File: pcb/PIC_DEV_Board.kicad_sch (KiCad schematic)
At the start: 8 parts, among them J1 Conn_01x08_Pin, J3 Conn_01x15_Pin, J4 Conn_01x02_Pin

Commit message: higher functionality board
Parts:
- removed J3: Conn_01x15_Pin, Connector_PinHeader_2.54mm:PinHeader_1x15_P2.54mm_Vertical, symbol Connector:Conn_01x15_Pin
- added C2, C3: 30pF, Capacitor_SMD:C_0805_2012Metric, symbol Device:C
- added C4, C6, C8: 0.1uF, Capacitor_SMD:C_0805_2012Metric, symbol Device:C
- added C5, C7, C9: 10uF, Capacitor_SMD:C_0805_2012Metric, symbol Device:C
- added D2, D3, D4, D5, D6, D7, D8, D9: LED, LED_SMD:LED_0805_2012Metric, symbol Device:LED
- added J2: USB_A, Connector_USB:USB_A_Receptacle_GCT_USB1046, symbol Connector:USB_A
- added R10, R4, R5, R6, R7, R8, R9: 10K, Resistor_SMD:R_0805_2012Metric, symbol Device:R
- added R11, R12, R13, R14, R15, R16, R17, R18: 560, Resistor_SMD:R_0805_2012Metric, symbol Device:R
- added R3: 0, Resistor_SMD:R_0805_2012Metric, symbol Device:R
- added U2: ~, Package_SO:SOIC-8_3.9x4.9mm_P1.27mm, symbol myCustomParts:AT24C01D
- added U3: MCP3002, Package_SO:SOIC-8_3.9x4.9mm_P1.27mm, symbol Analog_ADC:MCP3002
- added U4: MCP4801, Package_SO:SOIC-8_3.9x4.9mm_P1.27mm, symbol Analog_DAC:MCP4801
- added U5: FT230XS, Package_SO:SSOP-16_3.9x4.9mm_P0.635mm, symbol Interface_USB:FT230XS
- added U6: 74HC595, Package_SO:SOIC-16_3.9x9.9mm_P1.27mm, symbol 74xx:74HC595
- added Y1: Crystal, symbol Device:Crystal
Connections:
- net Earth: now also C2.1, C3.1, C4.2, C5.1, C6.2, C7.1, C8.2, C9.1, D2.1 (K), D3.1 (K), D4.1 (K), D5.1 (K), D6.1 (K), D7.1 (K), D8.1 (K), D9.1 (K), R10.1, R3.1, R8.1, R9.1, U2.4 (GND), U3.4 (VSS), U4.7 (Vss), U5.13 (GND), U5.5 (GND), U6.8 (GND)
- net +3V3: now reaches C1.2, J1.2 (Pin_2), J4.2 (Pin_2), R1.1, R2.1, U1.1 (Vdd)
- net +3V3: now also C4.1, C5.2, C6.1, C7.2, C8.1, C9.2, R4.1, R5.1, R6.1, R7.1, U2.8 (Vcc), U3.8 (VDD/VREF), U4.1 (Vdd), U5.12 (VCC), U6.16 (VCC)
- net Vpp/RA3/MCLR: now reaches R1.2, U1.4 (Vpp/RA3/MCLR)
- net Vpp/RA3/MCLR: no longer J1.1 (Pin_1)
- net at U1.2 (RA5): now also C2.2, Y1.2
- net at U1.16 (RC0): now also U5.4 (RXD)
- net at U1.15 (RC1): now also U6.14 (SER)
- net at U1.14 (RC2): now also U6.11 (SRCLK)
- net at U1.13 (RB4): now also U2.5 (SDA)
- net at U1.11 (RB6): now also U2.6 (SCL)
- net at U1.3 (RA4): now also C3.2, Y1.1
- net ~{DAC_CS}: now reaches U1.6 (RC4)
- net ~{DAC_CS}: now also U4.2 (~{CS})
- net ~{ADC_CS}: now reaches U1.7 (RC3)
- net ~{ADC_CS}: now also U3.1 (~{CS}/SHDN)
- net SCK: now reaches U1.8 (RC6)
- net SCK: now also U3.7 (CLK), U4.3 (SCK)
- net SDO: now reaches U1.9 (RC7)
- net SDO: now also U3.6 (DOUT)
- net SDI: now reaches U1.10 (RB7)
- net SDI: now also U3.5 (DIN), U4.4 (SDI)
- net at U1.17 (RA2): now also U5.1 (TXD)
- new net: D5.2 (A), R14.2
- new net: R6.2, R9.2, U2.2 (A1)
- new net: J2.3 (D+), U5.8 (USBDP)
- new net: J2.2 (D-), U5.9 (USBDM)
- new net: R14.1, U6.3 (QD)
- new net: R15.1, U6.4 (QE)
- new net: D6.2 (A), R15.2
- new net: R3.2, R4.2, U2.7 (WP)
- new net: D2.2 (A), R11.2
- new net: D4.2 (A), R13.2
- new net: R10.2, R7.2, U2.3 (A2)
- new net: D7.2 (A), R16.2
- new net: R16.1, U6.5 (QF)
- new net: D8.2 (A), R17.2
- new net: R5.2, R8.2, U2.1 (A0)
- new net: R13.1, U6.2 (QC)
- new net: R17.1, U6.6 (QG)
- new net: R11.1, U6.15 (QA)
- new net: R12.1, U6.1 (QB)
- new net: R18.1, U6.7 (QH)
- new net: D9.2 (A), R18.2
- new net: D3.2 (A), R12.2
- new net Vpp/RA3/MCLR: J1.1 (Pin_1)
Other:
- moved on the sheet: D1, J1, R1, R2

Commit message: size reduction
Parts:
- removed C2, C3: 30pF, Capacitor_SMD:C_0805_2012Metric, symbol Device:C
- removed D3, D4, D5, D6, D7, D8, D9: LED, LED_SMD:LED_0805_2012Metric, symbol Device:LED
- removed J2: USB_A, Connector_USB:USB_A_Receptacle_GCT_USB1046, symbol Connector:USB_A
- removed R10, R4, R5, R6, R7, R8, R9: 10K, Resistor_SMD:R_0805_2012Metric, symbol Device:R
- removed R11, R12, R13, R14, R15, R16, R17, R18: 560, Resistor_SMD:R_0805_2012Metric, symbol Device:R
- removed U6: 74HC595, Package_SO:SOIC-16_3.9x9.9mm_P1.27mm, symbol 74xx:74HC595
- removed Y1: Crystal, symbol Device:Crystal
- added J3: Conn_01x02_Pin, Connector_PinHeader_2.54mm:PinHeader_1x02_P2.54mm_Vertical, symbol Connector:Conn_01x02_Pin
- added J5: Conn_01x01_Pin, Connector_PinHeader_2.54mm:PinHeader_1x01_P2.54mm_Vertical, symbol Connector:Conn_01x01_Pin
- added U6: ~, myCustomFootprints:USB-A1HSB6, symbol myCustomParts:USB-A1HSB6
- R3: value 0 -> 1K
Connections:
- net Earth: now also U2.1 (A0), U2.2 (A1), U2.3 (A2), U2.7 (WP), U6.4 (GND); no longer R3.1
- net at U5.8 (USBDP): now also U6.3 (DP)
- net at U5.9 (USBDM): now also U6.2 (DM)
- net at R3.2: now also D2.2 (A); no longer U2.7 (WP)
- net at U4.8 (Vout): now also J5.1 (Pin_1)
- net at U1.2 (RA5): now also R3.1
- net at U3.2 (CH0): now also J3.1 (Pin_1)
- net at U3.3 (CH1): now also J3.2 (Pin_2)
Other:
- moved on the sheet: C4, C5, C6, C7, R1, U3, U4

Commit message: layout changes
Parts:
- added C2: 0.1uF, Capacitor_SMD:C_0805_2012Metric, symbol Device:C
- added R4: 10K, Resistor_SMD:R_0805_2012Metric, symbol Device:R
- added R5: 4.7K, Resistor_SMD:R_0805_2012Metric, symbol Device:R
- added TP1, TP2: TestPoint, TestPoint:TestPoint_Pad_1.5x1.5mm, symbol Connector:TestPoint
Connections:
- net Earth: now also C2.2, R4.1
- net at U1.17 (RA2), U5.1 (TXD): now also TP2.1
- net at U5.10 (3V3OUT): now also U5.11 (~{RESET}), U5.3 (VCCIO), C2.1
- net at U5.16 (CBUS3): now also R4.2, R5.1
- net at U1.16 (RC0), U5.4 (RXD): now also TP1.1
- net at U6.1 (VCC): now also R5.2

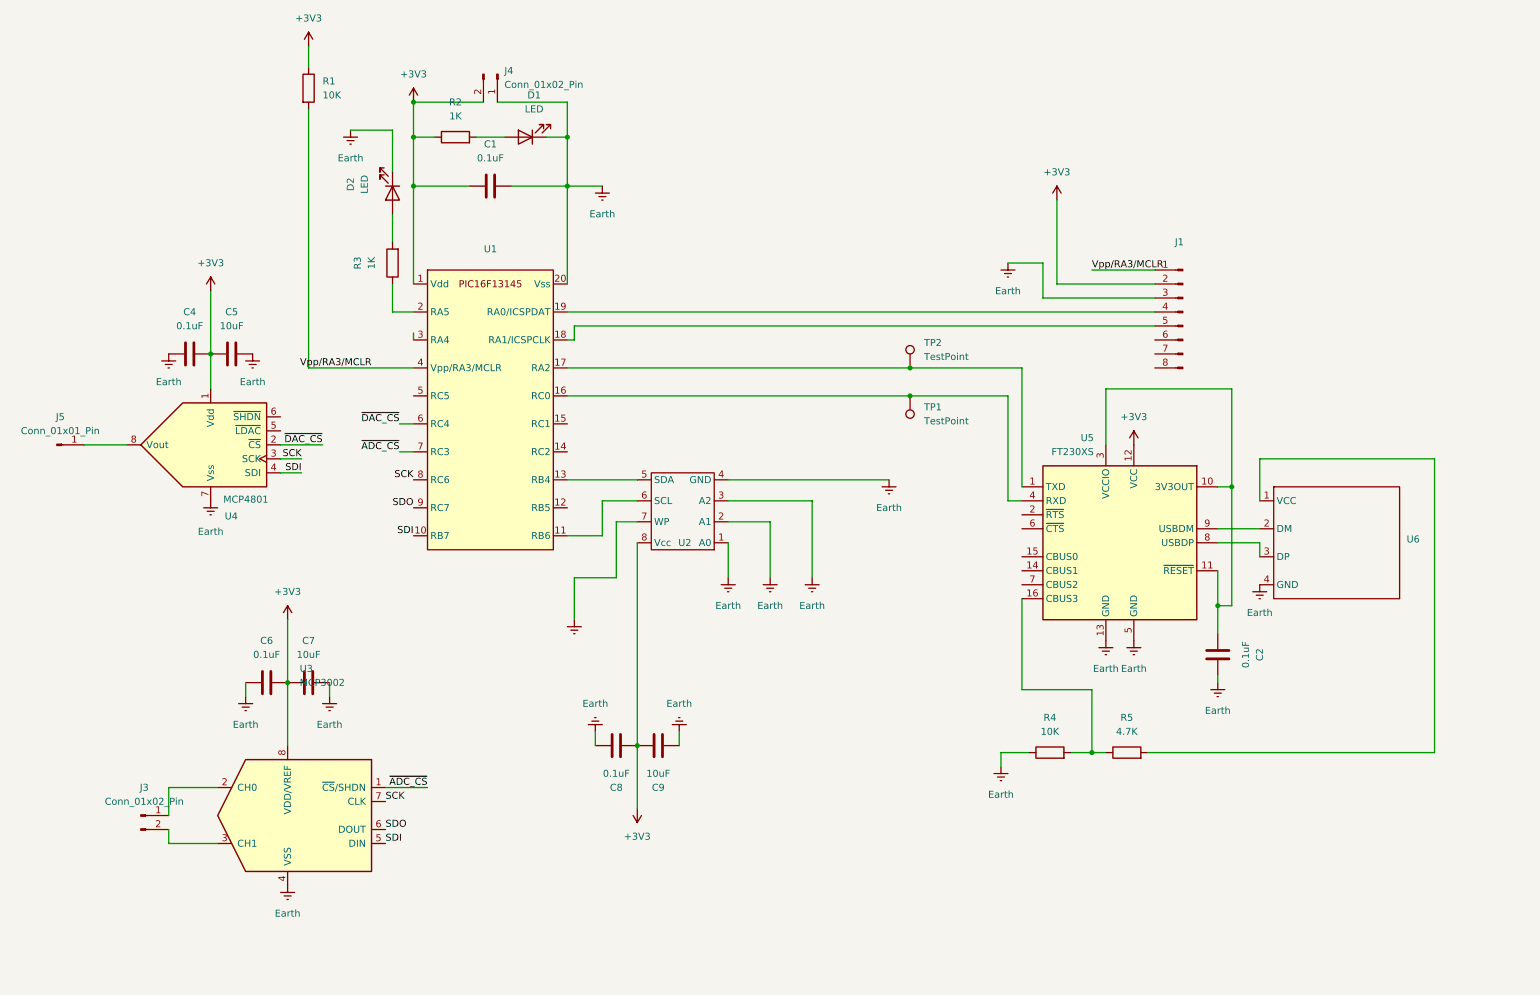
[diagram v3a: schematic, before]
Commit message: layout/schematic changes
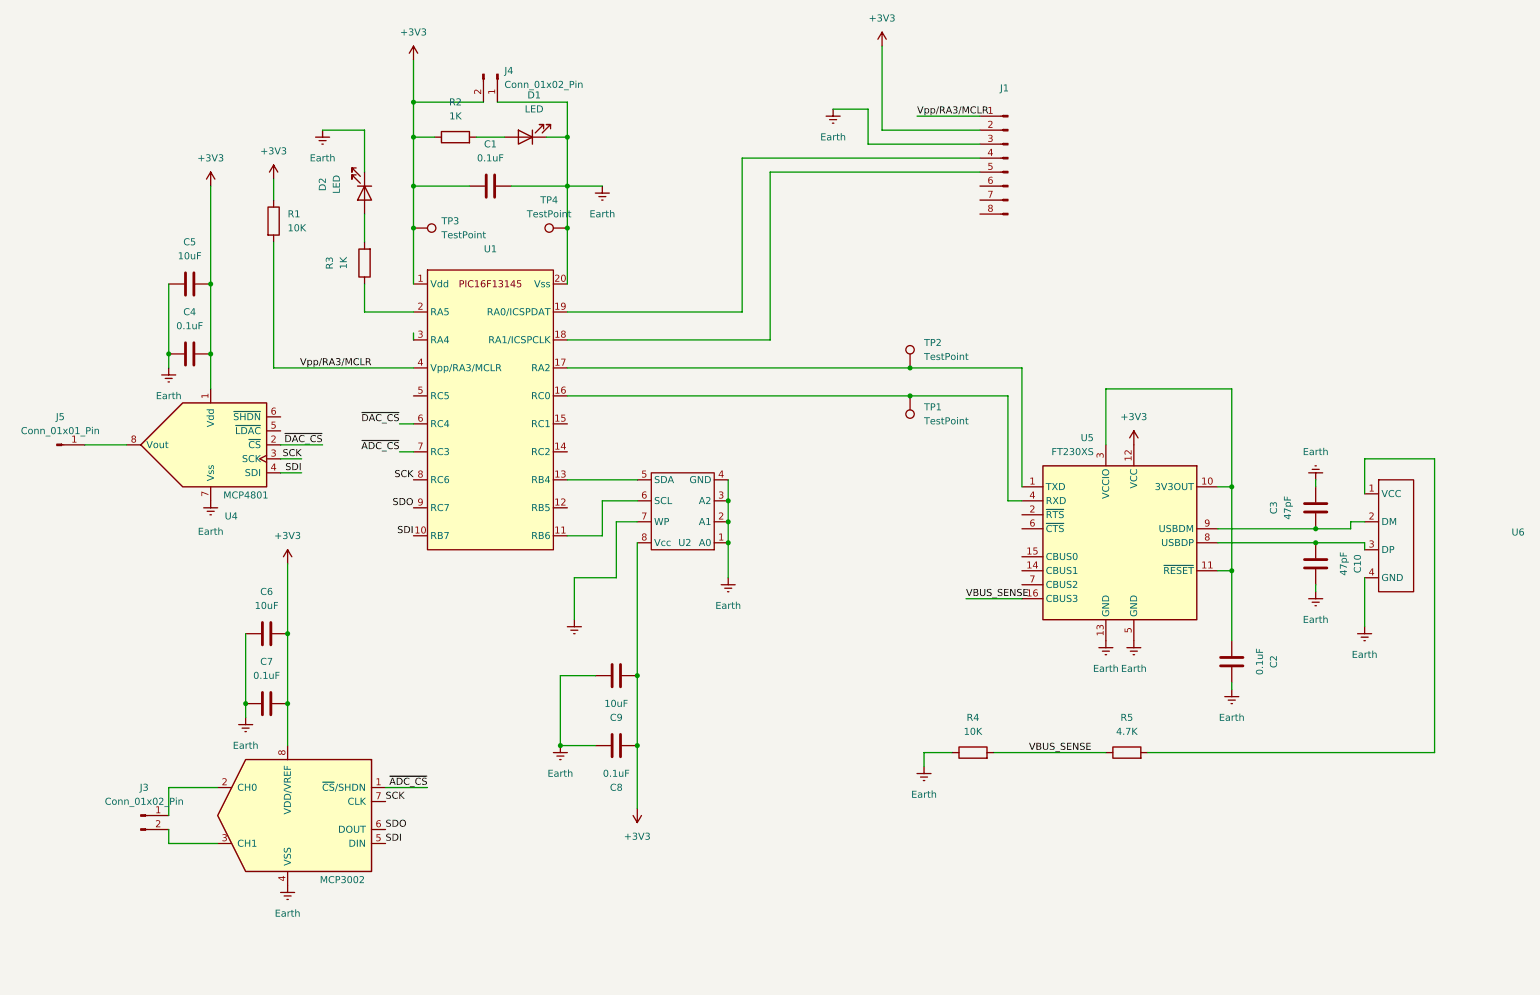
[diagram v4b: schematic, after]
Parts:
- added C10, C3: 47pF, Capacitor_SMD:C_0805_2012Metric, symbol Device:C
- added TP3, TP4: TestPoint, TestPoint:TestPoint_Pad_1.5x1.5mm, symbol Connector:TestPoint
- C6: value 0.1uF -> 10uF
- C7: value 10uF -> 0.1uF
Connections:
- net +3V3: now also C5.1, C7.1, C9.1, TP3.1; no longer C5.2, C7.2, C9.2
- net Earth: now also C5.2, C7.2, C9.2, C10.2, C3.2, TP4.1; no longer C5.1, C7.1, C9.1
- net VBUS_SENSE: now reaches R4.2, R5.1, U5.16 (CBUS3)
- net at U5.8 (USBDP), U6.3 (DP): now also C10.1
- net at U5.9 (USBDM), U6.2 (DM): now also C3.1
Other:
- moved on the sheet: C2, D2, J1, R1, R3, R4, U6

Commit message: layout/via changes
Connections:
- net Earth: now also U6.1 (GND); no longer U6.4 (GND)
- net at C10.1, U5.8 (USBDP): now also U6.2 (DP); no longer U6.3 (DP)
- net at C3.1, U5.9 (USBDM): now also U6.3 (DM); no longer U6.2 (DM)
- net at R5.2: now also U6.4 (VCC); no longer U6.1 (VCC)

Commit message: layout/via changes
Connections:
- net at U4.5 (~{LDAC}): now also U1.5 (RC5)
- net at U4.6 (~{SHDN}): now also U1.3 (RA4)
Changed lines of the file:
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@@
+	(wire
+		(pts
+			(xy 76.2 97.79) (xy 76.2 91.44)
+		)
+		(stroke
+			(width 0)
+			(type default)
+		)
+	)
 	(wire
 		(pts
@@
 	(wire
 		(pts
+			(xy 76.2 91.44) (xy 87.63 91.44)
+		)
+		(stroke
+			(width 0)
+			(type default)
+		)
+	)
+	(wire
+		(pts
 			(xy 115.57 116.84) (xy 121.92 116.84)
 		)
@@
 	(wire
 		(pts
+			(xy 87.63 81.28) (xy 83.82 81.28)
+		)
+		(stroke
+			(width 0)
+			(type default)
+		)
+	)
+	(wire
+		(pts
 			(xy 152.4 50.8) (xy 152.4 81.28)
 		)
@@
 	(wire
 		(pts
-			(xy 87.63 80.01) (xy 87.63 81.28)
-		)
-		(stroke
-			(width 0)
-			(type default)
-		)
-	)
-	(wire
-		(pts
 			(xy 118.11 142.24) (xy 118.11 154.94)
 		)
@@
 	(wire
 		(pts
+			(xy 83.82 90.17) (xy 63.5 90.17)
+		)
+		(stroke
+			(width 0)
+			(type default)
+		)
+	)
+	(wire
+		(pts
 			(xy 120.65 142.24) (xy 118.11 142.24)
 		)
@@
 	(wire
 		(pts
+			(xy 63.5 90.17) (xy 63.5 95.25)
+		)
+		(stroke
+			(width 0)
+			(type default)
+		)
+	)
+	(wire
+		(pts
 			(xy 52.07 172.72) (xy 43.18 172.72)
 		)
@@
 	(wire
 		(pts
+			(xy 63.5 97.79) (xy 76.2 97.79)
+		)
+		(stroke
+			(width 0)
+			(type default)
+		)
+	)
+	(wire
+		(pts
 			(xy 27.94 100.33) (xy 35.56 100.33)
 		)
@@
 		)
 		(stroke
+			(width 0)
+			(type default)
+		)
+	)
+	(wire
+		(pts
+			(xy 83.82 81.28) (xy 83.82 90.17)
+		)
+		(stroke
